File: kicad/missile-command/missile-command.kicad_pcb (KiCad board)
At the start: 2 copper layers, 300 x 300 mm, 14 parts

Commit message: Draw every device at its real package size
The board maps existed to answer "which chip is at C4", and then drew a
24-pin ROM and a 20-pin LS245 as the same 14-pin outline. package_for()
read pin counts from DEVICES, which holds 20 Pong-era parts against the
112 part types the boards actually use, and silently fell back to DIP-14
for the other 92.

tools/packages.py is the pin-count table, kept separate from devices.py
on purpose: packaging needs one number for every part on every board,
while devices.py carries verified pinouts for the parts validate_nets.py
reasons about, and widening that set to satisfy a drawing would let the
extractor trust readings nothing has checked.

688 of 704 devices now size. check_packages.py re-derives 56 of the
entries from KiCAD's symbol library — comparing the highest pin number,
not the pin count, since KiCAD omits no-connects and a 7493 symbol has
ten pins on a DIP-14 — and confirms all 20 parts in DEVICES agree. The
Am2901 slices and the POKEY come from DIP-40 stated on the Battlezone
sheet; the 8316E from the drawing's note that a 2708 may be fitted
instead.

What does not size is now said out loud rather than quietly drawn at 14
pins: four descriptions recorded where the sheet gave no part number,
and the Atari 0351xx ROM/PROM numbers, which get the class default and
are listed as unverified until someone has a board in front of them.

Two things found while reading the corpus for packages, both logged in
asteroids.read.json rather than acted on. The -06 rate multiplier
resolution was recorded and never applied to the board data, and the
parts list disagrees with both readings on designators. F4/H4/J4 take
either an LS670 or an LS170, and the 19-007 pull-up network is fitted
only with the LS170 — same package either way, but a real failure mode.

Also: republishing a board without --machine used to unlink it from its
machine, because most definitions carry no machine of their own and the
link lived only in boards.json. publish_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
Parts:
- UA4, UB4, UD5, UD6, UE5: footprint DIP-14_W7.62mm -> DIP-16_W7.62mm

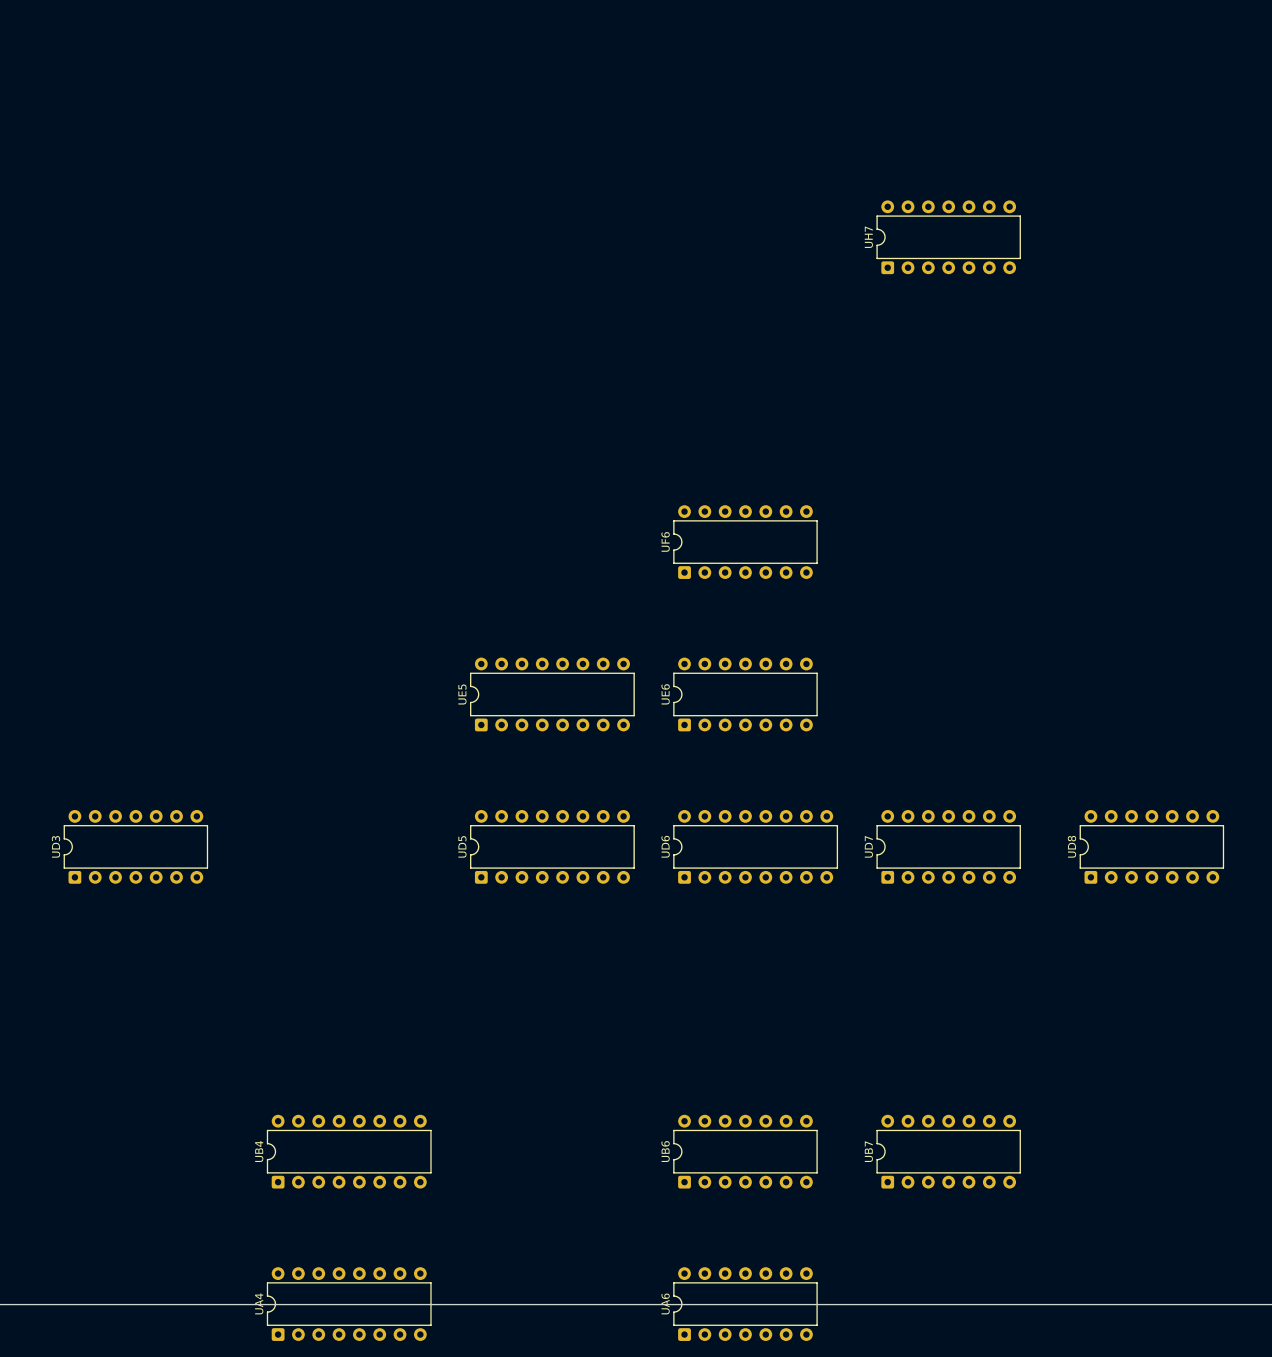
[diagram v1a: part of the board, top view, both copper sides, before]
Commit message: Drop two grid rows that do not exist, and span the devices that do
Atari's grid alphabet skips G, I, O and Q, and the board definitions
listed G and Q as rows. Every device below F was therefore drawn a row
too low, the rendered board carried two empty bands, and F/H1 looked
like a three-position span for a part 1.2in long on a 0.75in pitch.

Confirmed three ways before touching it. Nothing in any read, signature
or signal record in this repo sits in a G or Q row, while both
neighbours of each are populated on the two densest boards — Battlezone
P:6 R:2, Asteroids-03 P:4 R:3. The sheets' own spanning designators
treat F and H as adjacent and H and J as adjacent, which is only
possible if G and I are not positions. And with G removed, F/H falls out
as an adjacent pair, which is what a 24-pin ROM needs. Pong predates the
convention and legitimately uses G, so it keeps its grid.

Spans are now data rather than prose. A device drawn across two or three
cells is still keyed at its first cell, because that is the only thing
`ics` may be keyed by, but the sheet's own designator goes in a `spans`
map and the footprint is placed at the mean of the cells it names. A
DIP-40 at B/C2 sits between B2 and C2 instead of hanging equally over A2
and C2. The build rejects a span whose rows are not adjacent — that
failure almost always means the grid is wrong, not the span.

Two more inconsistencies found and logged rather than guessed at. Two of
the Math Box's four Am2901 slices carry a span and two do not, though
all four are the same DIP-40 on the same pitch. And asteroids-04.json
carries five devices at the -03 PROM positions alongside the -04 ROMs
and is missing 035144-02 at D/E1, contradicting the substitution table,
memory_by_revision and its own status text in the same breath.

Co-Authored-By: Claude Opus 5 <noreply@anthropic.com>
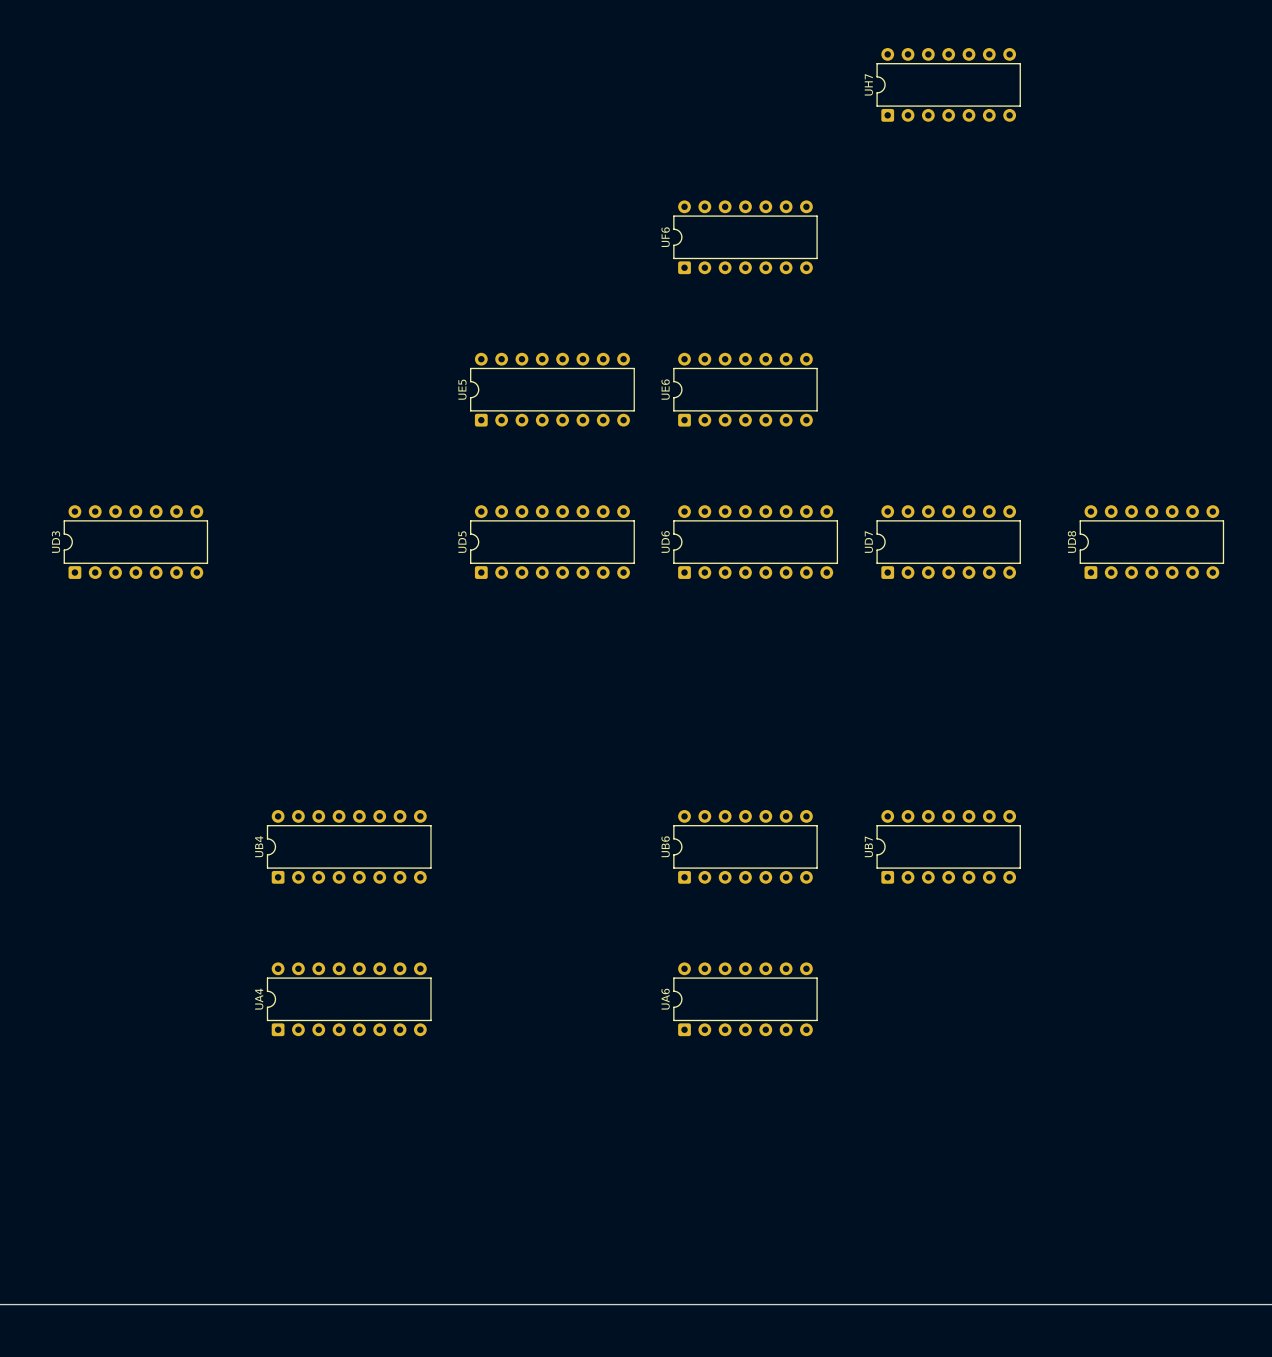
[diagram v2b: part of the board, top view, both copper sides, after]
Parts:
- moved UA4 38.1 mm to (102.2, 265.6)
- moved UA6 38.1 mm to (153.0, 265.6)
- moved UE5 38.1 mm to (127.6, 189.4)
- moved UE6 38.1 mm to (153.0, 189.4)
- moved UB4 38.1 mm to (102.2, 246.6)
- moved UB6 38.1 mm to (153.0, 246.6)
- moved UB7 38.1 mm to (178.4, 246.6)
- moved UD3 38.1 mm to (76.8, 208.5)
- moved UD5 38.1 mm to (127.6, 208.5)
- moved UD6 38.1 mm to (153.0, 208.5)
- moved UD7 38.1 mm to (178.4, 208.5)
- moved UD8 38.1 mm to (203.8, 208.5)
- moved UF6 38.1 mm to (153.0, 170.4)
- moved UH7 19.1 mm to (178.4, 151.3)

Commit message: Bring Missile Command and Lunar Lander through the same merge
Missile Command goes from 14 devices to 83, Lunar Lander from 6 to 60.
Both keep every device their drawing read already had, and every added
device records how many printings attest it.

Missile Command's five printings agree with each other on all 82
designators and confirm 12 of the 14 hand-read devices. The thirteenth,
D3, they dispute unanimously: all five call it a 74LS14 where the
drawing says 7404. The drawing keeps the cell, because the rule is that
a drawing read is someone looking at the board — but five against one is
worth knowing at the bench, so the dispute is now written into that
row's note and its source badge rather than buried in a log. The two
parts are both hex inverters on the same pinout, which is the pair a
drawing makes easiest to confuse.

Lunar Lander's three printings split on L6, E7 and E8 — some say
74LS170, others 74LS42, and a register file against a BCD decoder is not
a family misread, so one set is simply wrong and none of the three cells
is placed. Nine more designators appear in only one printing and are
left out; that manual's 1st printing carries 63 designators against the
3rd's 28, so those are mostly later printings not reprinting the list.

Two extraction fixes, both found by the packaging table refusing to size
what came out. Length was the wrong tie-break between two OCR readings
of a device name: '74S32' misread as '74832' is longer, and it parses as
a 74-series part with function number 832. What exposes it is that the
digits it actually ends in are 32, and 832 is not what follows a real
family — so the preference is now the spelling that decomposes as 74
plus a real family plus the device's own function number. That removed
74832, 74874 and 74L814 from three boards. The genuine parts the same
run surfaced — 7407, 74125, 74LS166, 74LS195, 74LS399 — join the
packaging table, verified against KiCAD, so all 901 devices still size.

Co-Authored-By: Claude Opus 5 <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
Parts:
- added UA1: 74LS244, DIP-20_W7.62mm, F.Cu at (26.0, 256.1)
- added UA5: 74S260, DIP-14_W7.62mm, F.Cu at (127.6, 265.6)
- added UA7: 7474, DIP-14_W7.62mm, F.Cu at (178.4, 265.6)
- added UA8: 74S00, DIP-14_W7.62mm, F.Cu at (203.8, 265.6)
- added UA9: 7474, DIP-14_W7.62mm, F.Cu at (229.2, 265.6)
- added UB1: 74LS244, DIP-20_W7.62mm, F.Cu at (26.0, 237.1)
- added UB5: 74LS10, DIP-14_W7.62mm, F.Cu at (127.6, 246.6)
- added UB8: 74S74, DIP-14_W7.62mm, F.Cu at (203.8, 246.6)
- added UC3: 7432, DIP-14_W7.62mm, F.Cu at (76.8, 227.6)
- added UC4: 74S32, DIP-14_W7.62mm, F.Cu at (102.2, 227.6)
- added UC5: 7400, DIP-14_W7.62mm, F.Cu at (127.6, 227.6)
- added UC7: 74LS175, DIP-16_W7.62mm, F.Cu at (178.4, 227.6)
- added UC8: 74S74, DIP-14_W7.62mm, F.Cu at (203.8, 227.6)
- added UD4: 7493, DIP-14_W7.62mm, F.Cu at (102.2, 208.5)
- added UD9: 74LS157, DIP-16_W7.62mm, F.Cu at (229.2, 208.5)
- added UE2: 74LS244, DIP-20_W7.62mm, F.Cu at (51.4, 189.4)
- added UE3: 74LS10, DIP-14_W7.62mm, F.Cu at (76.8, 189.4)
- added UE4: 74S157, DIP-16_W7.62mm, F.Cu at (102.2, 189.4)
- added UE7: 7474, DIP-14_W7.62mm, F.Cu at (178.4, 189.4)
- added UE8: 7442, DIP-16_W7.62mm, F.Cu at (203.8, 189.4)
- added UF2: 74LS244, DIP-20_W7.62mm, F.Cu at (51.4, 170.4)
- added UF3: 74153, DIP-16_W7.62mm, F.Cu at (76.8, 170.4)
- added UF5: 74LS153, DIP-16_W7.62mm, F.Cu at (127.6, 170.4)
- added UF7: 7474, DIP-14_W7.62mm, F.Cu at (178.4, 170.4)
- added UF9: 74LS273, DIP-20_W7.62mm, F.Cu at (229.2, 170.4)
- added UH2: 74LS157, DIP-16_W7.62mm, F.Cu at (51.4, 151.3)
- added UH3: 74153, DIP-16_W7.62mm, F.Cu at (76.8, 151.3)
- added UH5: 74LS153, DIP-16_W7.62mm, F.Cu at (127.6, 151.3)
- added UH6: 7474, DIP-14_W7.62mm, F.Cu at (153.0, 151.3)
- added UJ2: 74LS157, DIP-16_W7.62mm, F.Cu at (51.4, 132.3)
- added UJ3: 74153, DIP-16_W7.62mm, F.Cu at (76.8, 132.3)
- added UJ5: 74LS153, DIP-16_W7.62mm, F.Cu at (127.6, 132.3)
- added UJ6: 74LS08, DIP-14_W7.62mm, F.Cu at (153.0, 132.3)
- added UJ7: 74LS32, DIP-14_W7.62mm, F.Cu at (178.4, 132.3)
- added UJ8: 7474, DIP-14_W7.62mm, F.Cu at (203.8, 132.3)
- added UJ9: 74LS14, DIP-14_W7.62mm, F.Cu at (229.2, 132.3)
- added UK2: 74LS157, DIP-16_W7.62mm, F.Cu at (51.4, 113.2)
- added UK3: 74153, DIP-16_W7.62mm, F.Cu at (76.8, 113.2)
- added UK5: 74LS153, DIP-16_W7.62mm, F.Cu at (127.6, 113.2)
- added UK6: 74S32, DIP-14_W7.62mm, F.Cu at (153.0, 113.2)
- added UK7: 7404, DIP-14_W7.62mm, F.Cu at (178.4, 113.2)
- added UK8: 74LS191, DIP-16_W7.62mm, F.Cu at (203.8, 113.2)
- added UK9: 74LS191, DIP-16_W7.62mm, F.Cu at (229.2, 113.2)
- added UL2: 74LS157, DIP-16_W7.62mm, F.Cu at (51.4, 94.2)
- added UL5: 74S32, DIP-14_W7.62mm, F.Cu at (127.6, 94.2)
- added UL8: 74175, DIP-16_W7.62mm, F.Cu at (203.8, 94.2)
- added UL9: 74LS244, DIP-20_W7.62mm, F.Cu at (229.2, 94.2)
- added UM2: 74LS157, DIP-16_W7.62mm, F.Cu at (51.4, 75.2)
- added UM3: 74S08, DIP-14_W7.62mm, F.Cu at (76.8, 75.2)
- added UM5: 74LS139, DIP-16_W7.62mm, F.Cu at (127.6, 75.2)
- added UM6: 74LS195, DIP-16_W7.62mm, F.Cu at (153.0, 75.2)
- added UM7: 74LS157, DIP-16_W7.62mm, F.Cu at (178.4, 75.2)
- added UM9: 74LS244, DIP-20_W7.62mm, F.Cu at (229.2, 75.2)
- added UN11: 7407, DIP-14_W7.62mm, F.Cu at (280.0, 56.1)
- added UN2: 7442, DIP-16_W7.62mm, F.Cu at (51.4, 56.1)
- added UN3: 74LS244, DIP-20_W7.62mm, F.Cu at (76.8, 46.6)
- added UN5: 74LS251, DIP-16_W7.62mm, F.Cu at (127.6, 56.1)
- added UN6: 74LS273, DIP-20_W7.62mm, F.Cu at (153.0, 56.1)
- added UN7: 74LS195, DIP-16_W7.62mm, F.Cu at (178.4, 56.1)
- added UP10: 74LS244, DIP-20_W7.62mm, F.Cu at (254.6, 37.0)
- added UP2: 74LS139, DIP-16_W7.62mm, F.Cu at (51.4, 37.0)
- added UP5: 74LS244, DIP-20_W7.62mm, F.Cu at (127.6, 37.0)
- added UP6: 74LS166, DIP-16_W7.62mm, F.Cu at (153.0, 37.0)
- added UP7: 74LS153, DIP-16_W7.62mm, F.Cu at (178.4, 37.0)
- added UR2: 74LS08, DIP-14_W7.62mm, F.Cu at (51.4, 18.0)
- added UR4: 74LS163A, DIP-16_W7.62mm, F.Cu at (102.2, 18.0)
- added UR5: 7432, DIP-14_W7.62mm, F.Cu at (127.6, 18.0)
- added UR6: 74125, DIP-14_W7.62mm, F.Cu at (153.0, 18.0)
- added UR7: 7475, DIP-16_W7.62mm, F.Cu at (178.4, 18.0)

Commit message: Settle four gaps from outside sources, and find a fifth inside
Researching the open questions turned up a source that was in the corpus
all along. Atari stocked IC sockets by contact count, so a parts list
row like '79-42C24 24-Contact Medium-Insertion-Force Integrated Circuit
Socket (J2, H2, E/F2, N/P3)' states the pin count of every socketed
position, in the same typeset list the devices come from.
check_socket_pins.py checks packages.py against it: 26 sizes confirmed,
none contradicted. It needs the same --docs and --figure targeting the
merge does — pooled by machine it mixes Battlezone's two PCBs and
compares one printing's numbering against another's, and reported
thirteen contradictions that were all artefacts of that.

The Atari ROM sizes are no longer a class default. Those sockets are the
program ROM and vector ROM positions, and they are 24-contact.

The -05/-06 ROM positions were the wrong way round. 035143-02 is at J2
and 035145-02 at E/F2, not the reverse. Three sources agree and two are
in this corpus: the 6th and 7th printings both list the positions
outright, and MAME's asteroid driver names its dumps 035143-02.j2 and
035145-04e.ef2, its suffixes being board positions checked against real
boards. 035144-02 at H2 was right all along; only the outer two were
swapped.

The twelfth -03 PROM is real and is in — 035142-02 at L1, with 035155-02
as its alternate. Sheet 01B of the 4th-printing drawing package carries
'035142-01 L1' directly, which is the drawing rather than a manual
quoting it, six further documents repeat it, and the memory map requires
it: 6800-7FFF is 6144 bytes, exactly twelve 512-byte PROMs or three 2K
ROMs and nothing else that tiles evenly. Eleven could never have been
right.

Missile Command D3 is a 74LS14 and the 7404 reading is withdrawn. All
five printings give '37-74LS14 Type 74LS14 Integrated Circuit (D3)' with
stock number and description agreeing in each, and the same rows put a
plain 7414 at J9, so the lists distinguish the t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
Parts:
- UD3: value 7404 -> 74LS14

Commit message: Place the memory devices the IC parts lists cannot reach
Atari stocks ROM, RAM and the microprocessor under its own part numbers
— 90-7033, 036175-01, 90-6013 — not as 37-series IC stock, so the IC
harvest cannot see them however well it reads. That is why Centipede's
ROMs were missing and Red Baron's map had ten devices. merge_memory.py
reads those rows from the same typeset parts lists, under the same rules
as the IC merge: the drawing wins where it exists, two documents must
agree, and nothing is placed whose package cannot be established.

Red Baron 10 to 15, Asteroids Deluxe 92 to 100, Tempest 83 to 88,
Centipede 93 to 95, Missile Command 83 to 85, Lunar Lander 60 to 62.
1,494 devices across the boards, all sized, none contradicted.

Establishing the packages took two corrections, and both were the same
mistake in different clothes.

The first attempt sized Atari stock numbers by correlating a part
against the contact count of the socket at the positions it occupies,
pooled across a machine's documents. That is not a near miss: it put the
2114 at 40 pins, on twelve positions of apparent evidence, because two
printings number the board differently and the correlation was reading
one printing's parts list against another's sockets. Confined to within
a single document it behaves — 33 stock numbers established, 90-6013 by
39 documents agreeing, and 90-7033 correctly refusing to answer rather
than answering wrongly. Those 33 are in packages.py with their
provenance.

The second was the same shape. MAME's dump size was sizing a part from
whatever MAME dumped at that cell, which on Red Baron meant sizing
036175-01 from a dump of 037000-01 — sizing the socket, not the chip.
MAME now sizes a part only when the dump is of that part. Red Baron
loses two devices and keeps thirteen that are right.

Four more parts are sized from MAME's dump sizes alone, where every set
carrying the part agrees and the era leaves no room: 32 bytes and 256
bytes are both bipolar PROMs in a 1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
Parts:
- added UC2: 90-6013, DIP-40_W15.24mm, F.Cu at (51.4, 227.6)
- added UL6: 035826-01, DIP-16_W7.62mm, F.Cu at (153.0, 94.2)
